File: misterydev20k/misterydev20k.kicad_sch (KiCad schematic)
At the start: 55 parts, among them J1 SWD, J2 USB_C_Receptacle_USB2.0, SW1 Boot, U1 SY8113BADC, U2 W25Q128JVS, U3 USBLC6-2SC6, U4 RP2040, Y1 12MHz

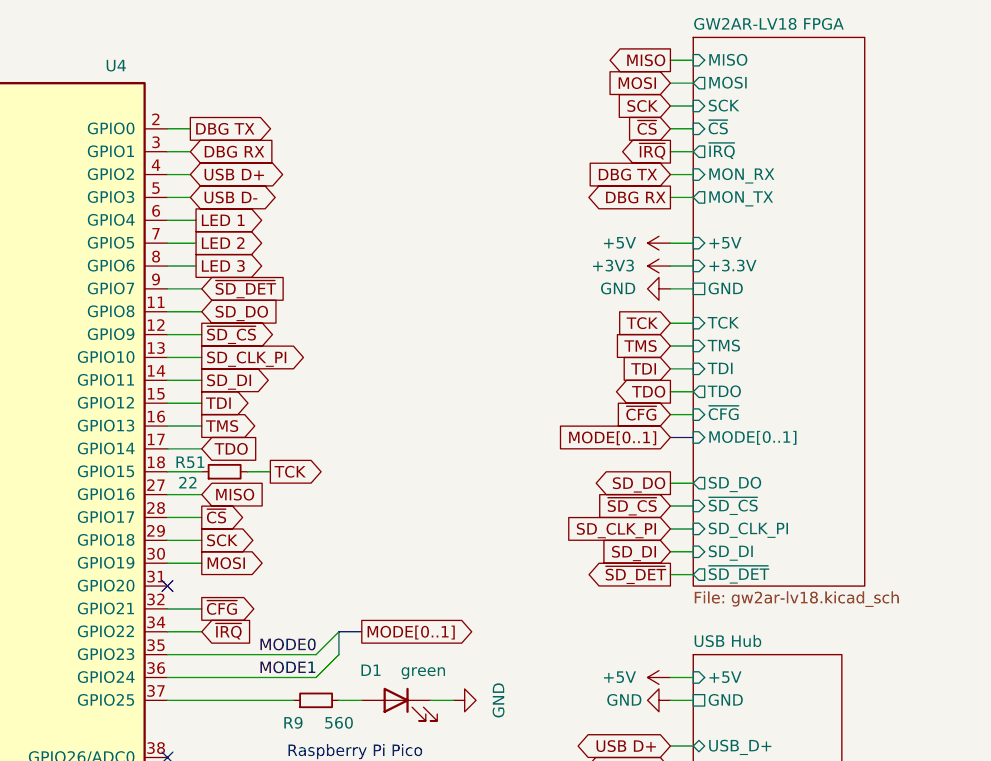
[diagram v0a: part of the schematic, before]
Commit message: Update dev20k pinout
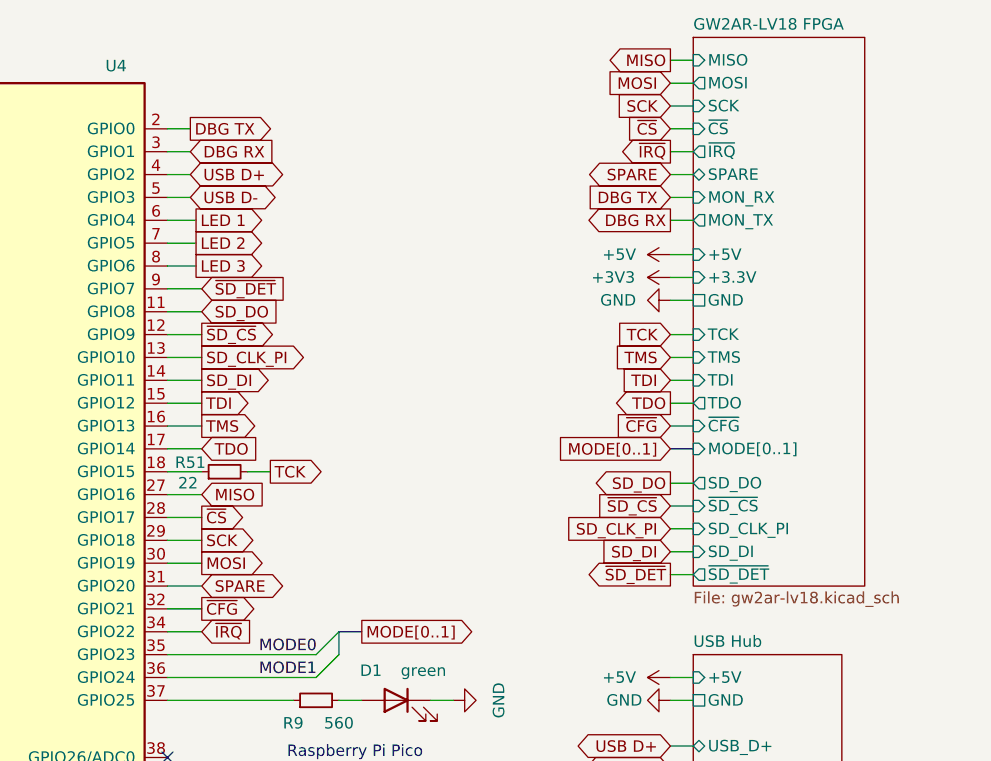
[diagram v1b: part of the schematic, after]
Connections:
- net SPARE: now reaches U4.31 (GPIO20)
- no-connect marks 7 -> 6
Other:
- sheet GW2AR-LV18 FPGA ports: added SPARE; removed none

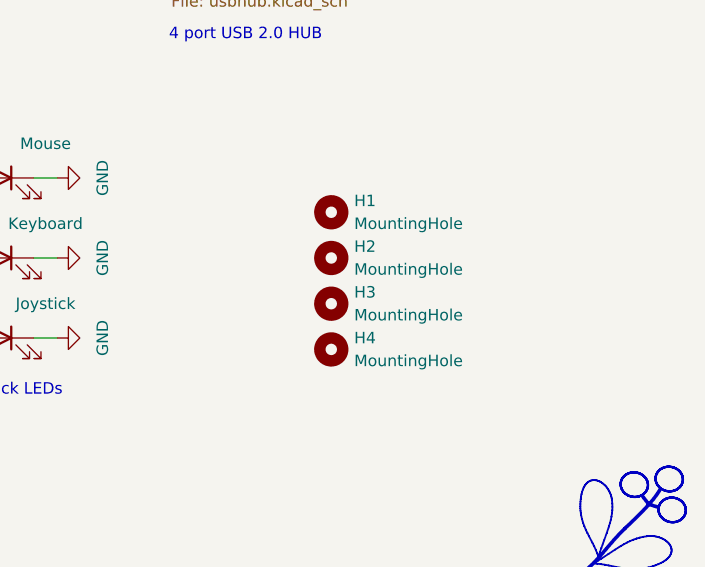
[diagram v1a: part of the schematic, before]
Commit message: Dev20k LCSC part mapping
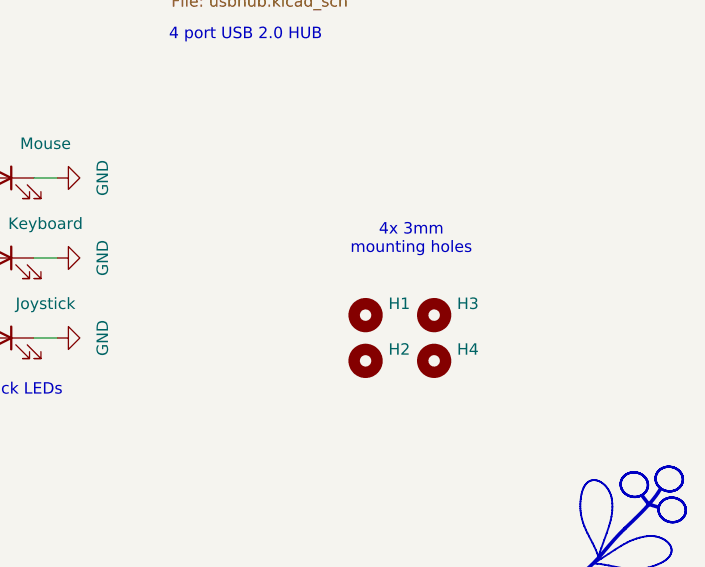
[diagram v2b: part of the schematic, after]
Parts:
- C1, C6, C8: Comment (none) -> Samsung 25V X5R; LCSC C52923 -> (none); LCSC Part # (none) -> C52923; checked (none) -> once
- C10, C9: LCSC C1555 -> (none); LCSC Part # (none) -> C1555; checked (none) -> once
- C11, C12, C13, C14, C2, C3, C5, C51, C54: LCSC C1525 -> (none); LCSC Part # (none) -> C1525; checked (none) -> once
- C52, C57: LCSC C1525 -> (none); LCSC Part # (none) -> C14663; checked (none) -> once
- C53: Comment (none) -> Samsung 10V X5R; LCSC C52923 -> (none); LCSC Part # (none) -> C19702; checked (none) -> once
- C55: LCSC C1525 -> (none); LCSC Part # (none) -> C1555; checked (none) -> once
- C56: Comment (none) -> Murata 10V X5R; LCSC C52923 -> (none); LCSC Part # (none) -> C84419; checked (none) -> once
- C7: Comment (none) -> Samsung 6.3V X5R; LCSC C15525 -> (none); LCSC Part # (none) -> C15525; checked (none) -> once
- D1, D2, D3, D4: LCSC C2297 -> (none); LCSC Part # (none) -> C2297; checked (none) -> once
- J1: footprint Connector_PinSocket_2.54mm:PinSocket_1x05_P2.54mm_Vertical -> Connector_PinHeader_2.54mm:PinHeader_1x05_P2.54mm_Vertical; LCSC Part # (none) -> C492404; checked (none) -> once
- J2: LCSC C165948 -> (none); LCSC Part # (none) -> C165948; checked (none) -> once
- L3: LCSC C408336 -> (none); LCSC Part # (none) -> C408336; checked (none) -> once
- R1, R53, R6, R7: LCSC C11702 -> (none); LCSC Part # (none) -> C11702; checked (none) -> once
- R10, R11, R12: LCSC Part # (none) -> C163460; checked (none) -> once
- R2, R3: LCSC C25905 -> (none); LCSC Part # (none) -> C25905; checked (none) -> once
- R4, R5: LCSC C25190 -> (none); LCSC Part # (none) -> C25190; checked (none) -> once
- R51: LCSC C163460 -> (none); LCSC Part # (none) -> C25092; checked (none) -> once
- R54: LCSC C11702 -> (none); LCSC Part # (none) -> C25756; checked (none) -> once
- R55: LCSC C11702 -> (none); LCSC Part # (none) -> C25890; checked (none) -> once
- R8: LCSC C11702 -> (none); LCSC Part # (none) -> C138008; checked (none) -> once
- R9: LCSC C163460 -> (none); LCSC Part # (none) -> C163460; checked (none) -> once
- SW1: LCSC C318884 -> (none); LCSC Part # (none) -> C318884; checked (none) -> once
- U1: LCSC Part # (none) -> C78989; checked (none) -> once
- U2: LCSC C131025 -> (none); LCSC Part # (none) -> C131025; checked (none) -> once
- U3: LCSC C2827654 -> (none); LCSC Part # (none) -> C2827654; checked (none) -> once
- U4: LCSC C2040 -> (none); checked (none) -> once
- Y1: Comment (none) -> SMD 3225 4-Pin; LCSC C9002 -> (none); checked (none) -> once
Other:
- note added: "4x 3mm mounting holes"
- moved on the sheet: H1, H2, H3, H4

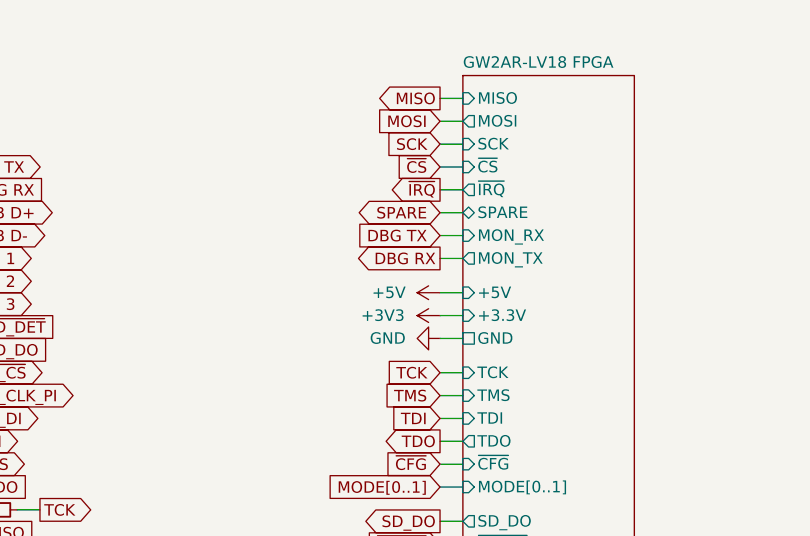
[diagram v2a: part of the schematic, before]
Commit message: Update debug UART wiring
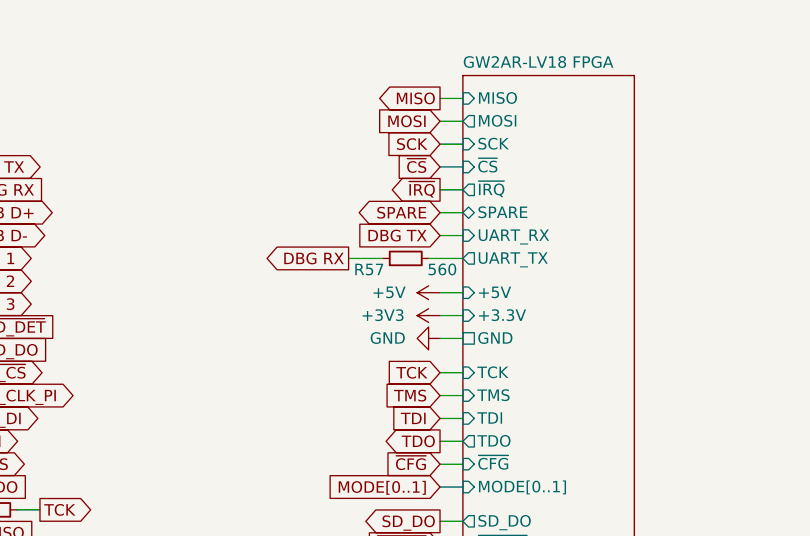
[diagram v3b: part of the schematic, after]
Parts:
- added R57: 560, Resistor_SMD:R_0402_1005Metric, symbol Device:R_Small
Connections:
- net DBG RX: now also R57.1
- new net GW2AR-LV18 FPGA/UART_TX: R57.2
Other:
- sheet GW2AR-LV18 FPGA ports: added UART_RX, UART_TX; removed MON_RX, MON_TX
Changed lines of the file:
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@@
 	(wire
 		(pts
-			(xy 223.52 50.8) (xy 226.06 50.8)
+			(xy 222.25 50.8) (xy 226.06 50.8)
 		)
 		(stroke
@@
 	(wire
 		(pts
+			(xy 217.17 50.8) (xy 213.36 50.8)
+		)
+		(stroke
+			(width 0)
+			(type default)
+		)
+	)
+	(wire
+		(pts
 			(xy 200.66 144.78) (xy 203.2 144.78)
 		)
@@
 	(global_label "DBG RX"
 		(shape output)
-		(at 223.52 50.8 180)
+		(at 213.36 50.8 180)
 		(fields_autoplaced yes)
 		(effects
@@
 		)
 		(property "Intersheetrefs" "${INTERSHEET_REFS}"
-			(at 213.9319 50.8 0)
+			(at 203.7719 50.8 0)
 			(effects
 				(font
@@
 	)
 	(symbol
+		(lib_id "Device:R_Small")
+		(at 219.71 50.8 90)
+		(unit 1)
+		(exclude_from_sim no)
+		(in_bom yes)
+		(on_board yes)
+		(dnp no)
+		(property "Reference" "R57"
+			(at 215.646 52.07 90)
+			(effects
+				(font
+					(size 1.27 1.27)
+				)
+			)
+		)
+		(property "Value" "560"
+			(at 223.774 52.07 90)
+			(effects
+				(font
+					(size 1.27 1.27)
+				)
+			)
+		)
+		(property "Footprint" "Resistor_SMD:R_0402_1005Metric"
+			(at 219.71 50.8 0)
+			(effects
+				(font
+					(size 1.27 1.27)
+				)
+				(hide yes)
+			)
+		)
+		(property "Datasheet" "~"
+			(at 219.71 50.8 0)
+			(effects
+				(font
+					(size 1.27 1.27)
+				)
+				(hide yes)
+			)
+		)
+		(property "Description" ""
+			(at 219.71 50.8 0)
+			(effects
+				(font
+					(size 1.27 1.27)
+				)
+				(hide yes)
+			)
+		)
+		(property "checked" "once"
+			(at 219.71 50.8 90)
+			(effects
+				(font
+					(size 1.27 1.27)
+				)
+				(hide yes)
+			)
+		)
+		(property "LCSC Part #" "C163460"
+			(at 219.71 50.8 90)
+			(effects
+				(font
+					(size 1.27 1.27)
+				)
+				(hide yes)
+			)
+		)
+		(pin "1"
+		)
+		(pin "2"
+		)
+		(instances
+			(project "misterydev20k"
+				(path "/ba62e47e-9e07-4e97-ab08-24b670d50f97"
+					(reference "R57")
+					(unit 1)
+				)
+			)
+		)
+	)
+	(symbol
 		(lib_id "Device:C_Small")
 		(at 88.9 184.15 0)
@@
 			)
 		)
-		(pin "MON_RX" input
+		(pin "UART_RX" input
 			(at 226.06 48.26 180)
 			(effects
@@
 			)
 		)
-		(pin "MON_TX" output
+		(pin "UART_TX" output
 			(at 226.06 50.8 180)
 			(effects

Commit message: Fix JLCPCB footprint offset and rotation
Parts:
- J1, U3: FT Rotation Offset (none) -> 90
- J2: FT Position Offset (none) -> 0,2
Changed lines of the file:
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@@
 			)
 		)
+		(property "FT Rotation Offset" "90"
+			(at 83.82 62.23 90)
+			(effects
+				(font
+					(size 1.27 1.27)
+				)
+				(hide yes)
+			)
+		)
 		(pin "1"
 		)
@@
 			)
 		)
+		(property "FT Rotation Offset" "90"
+			(at 34.29 140.97 0)
+			(effects
+				(font
+					(size 1.27 1.27)
+				)
+				(hide yes)
+			)
+		)
 		(pin "1"
 		)
@@
 			(at 48.26 49.53 0)
 			(effects
+				(font
+					(size 1.27 1.27)
+				)
+				(hide yes)
+			)
+		)
+		(property "FT Position Offset" "0,2"
+			(at 48.26 49.53 0)
+			(effects

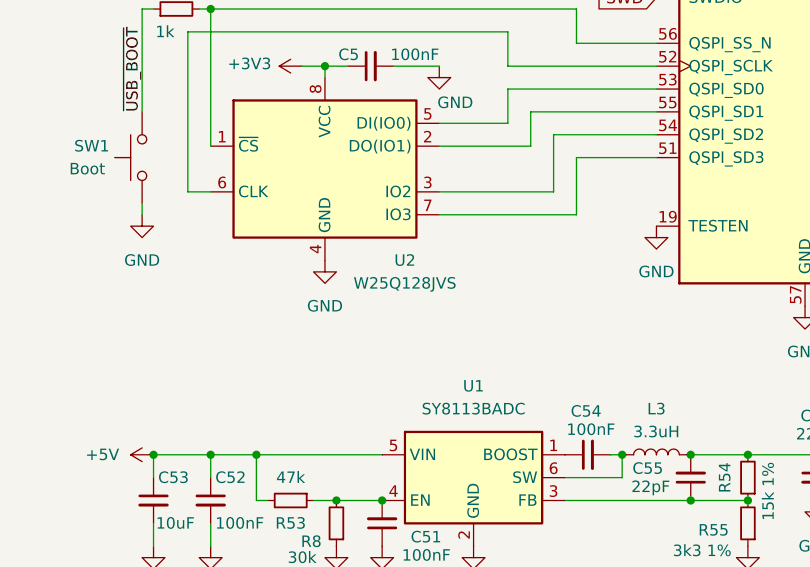
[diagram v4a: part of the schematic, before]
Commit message: Update misterydev20k to v1.1
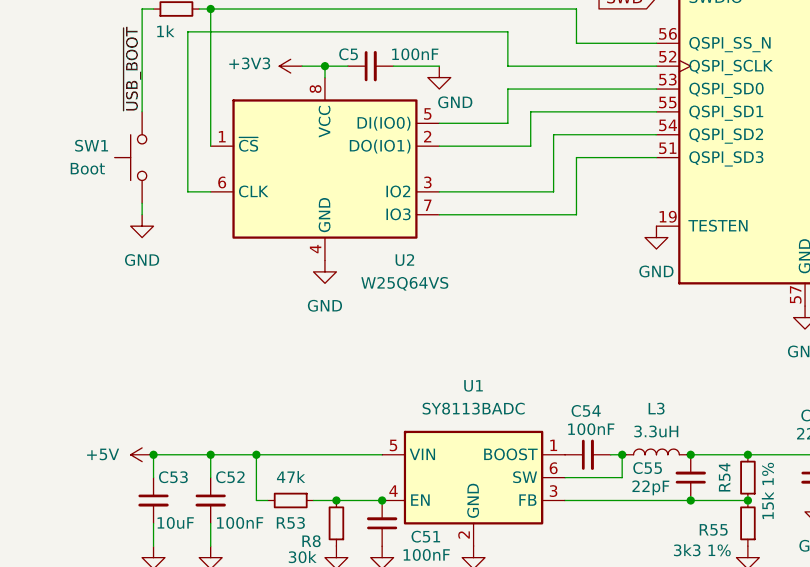
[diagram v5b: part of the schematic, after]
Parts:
- U2: value W25Q128JVS -> W25Q64VS
